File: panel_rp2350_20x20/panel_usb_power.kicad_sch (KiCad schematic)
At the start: 4 parts, among them J1 Conn_01x04, U39 AP2112K-3.3

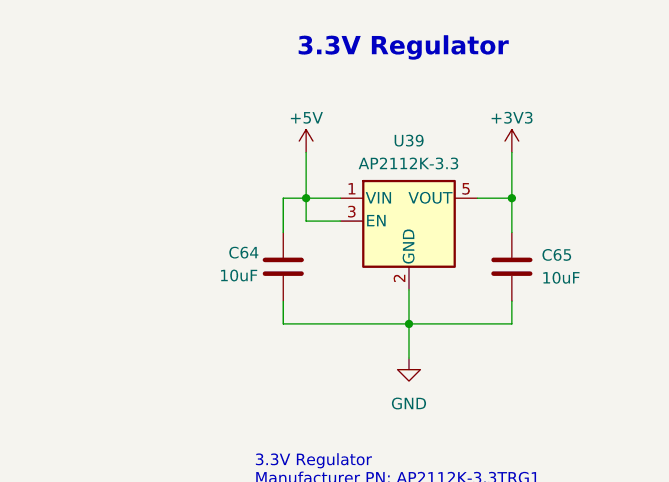
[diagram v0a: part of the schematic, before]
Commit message: More work on rp2350 20x20 panel.
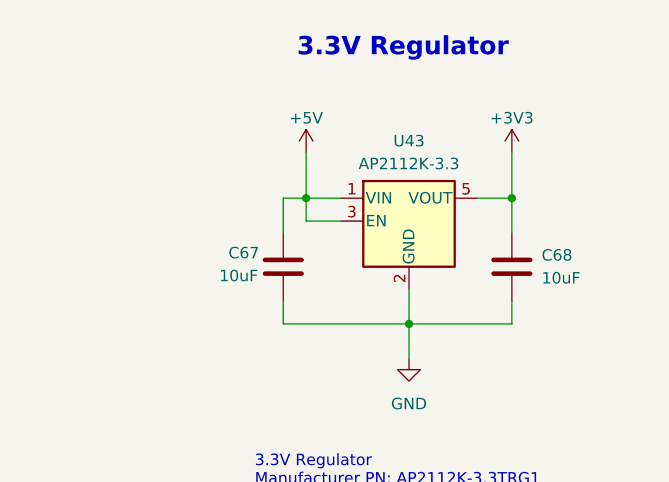
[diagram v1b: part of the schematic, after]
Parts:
- renumbered C64 to C67, C65 to C68, U39 to U43
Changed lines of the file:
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@@
 		(dnp no)
 		(fields_autoplaced yes)
-		(property "Reference" "#PWR0110"
+		(property "Reference" "#PWR0118"
 			(at 100.965 59.69 0)
 			(effects
@@
 			(project "driver_rp2350"
 				(path "/1e634561-32a0-4ffa-9d4f-e93f355464d5/e614504e-e15b-412a-a899-de4ba0827a39"
-					(reference "#PWR0110")
+					(reference "#PWR0118")
 					(unit 1)
 				)
@@
 		(dnp no)
 		(fields_autoplaced yes)
-		(property "Reference" "#PWR0113"
+		(property "Reference" "#PWR0121"
 			(at 226.06 44.45 0)
 			(effects
@@
 			(project "driver_rp2350"
 				(path "/1e634561-32a0-4ffa-9d4f-e93f355464d5/e614504e-e15b-412a-a899-de4ba0827a39"
-					(reference "#PWR0113")
+					(reference "#PWR0121")
 					(unit 1)
 				)
@@
 		(on_board yes)
 		(dnp no)
-		(property "Reference" "#PWR0109"
+		(property "Reference" "#PWR0117"
 			(at 100.965 48.895 0)
 			(effects
@@
 			(project "driver_rp2350"
 				(path "/1e634561-32a0-4ffa-9d4f-e93f355464d5/e614504e-e15b-412a-a899-de4ba0827a39"
-					(reference "#PWR0109")
+					(reference "#PWR0117")
 					(unit 1)
 				)
@@
 		(on_board yes)
 		(dnp no)
-		(property "Reference" "#PWR0111"
+		(property "Reference" "#PWR0119"
 			(at 203.2 44.45 0)
 			(effects
@@
 			(project "driver_rp2350"
 				(path "/1e634561-32a0-4ffa-9d4f-e93f355464d5/e614504e-e15b-412a-a899-de4ba0827a39"
-					(reference "#PWR0111")
+					(reference "#PWR0119")
 					(unit 1)
 				)
@@
 		(on_board yes)
 		(dnp no)
-		(property "Reference" "C64"
+		(property "Reference" "C67"
 			(at 194.564 51.816 0)
 			(effects
@@
 			(project "driver_rp2350"
 				(path "/1e634561-32a0-4ffa-9d4f-e93f355464d5/e614504e-e15b-412a-a899-de4ba0827a39"
-					(reference "C64")
+					(reference "C67")
 					(unit 1)
 				)
@@
 		(on_board yes)
 		(dnp no)
-		(property "Reference" "C65"
+		(property "Reference" "C68"
 			(at 229.362 52.07 0)
 			(effects
@@
 			(project "driver_rp2350"
 				(path "/1e634561-32a0-4ffa-9d4f-e93f355464d5/e614504e-e15b-412a-a899-de4ba0827a39"
-					(reference "C65")
+					(reference "C68")
 					(unit 1)
 				)
@@
 		(dnp no)
 		(fields_autoplaced yes)
-		(property "Reference" "U39"
+		(property "Reference" "U43"
 			(at 214.63 39.37 0)
 			(effects
@@
 			(project "driver_rp2350"
 				(path "/1e634561-32a0-4ffa-9d4f-e93f355464d5/e614504e-e15b-412a-a899-de4ba0827a39"
-					(reference "U39")
+					(reference "U43")
 					(unit 1)
 				)
@@
 		(dnp no)
 		(fields_autoplaced yes)
-		(property "Reference" "#PWR0112"
+		(property "Reference" "#PWR0120"
 			(at 214.63 69.85 0)
 			(effects
@@
 			(project "driver_rp2350"
 				(path "/1e634561-32a0-4ffa-9d4f-e93f355464d5/e614504e-e15b-412a-a899-de4ba0827a39"
-					(reference "#PWR0112")
-					(unit 1)
-				)
+					(reference "#PWR0120")
+					(unit 1)
+				)

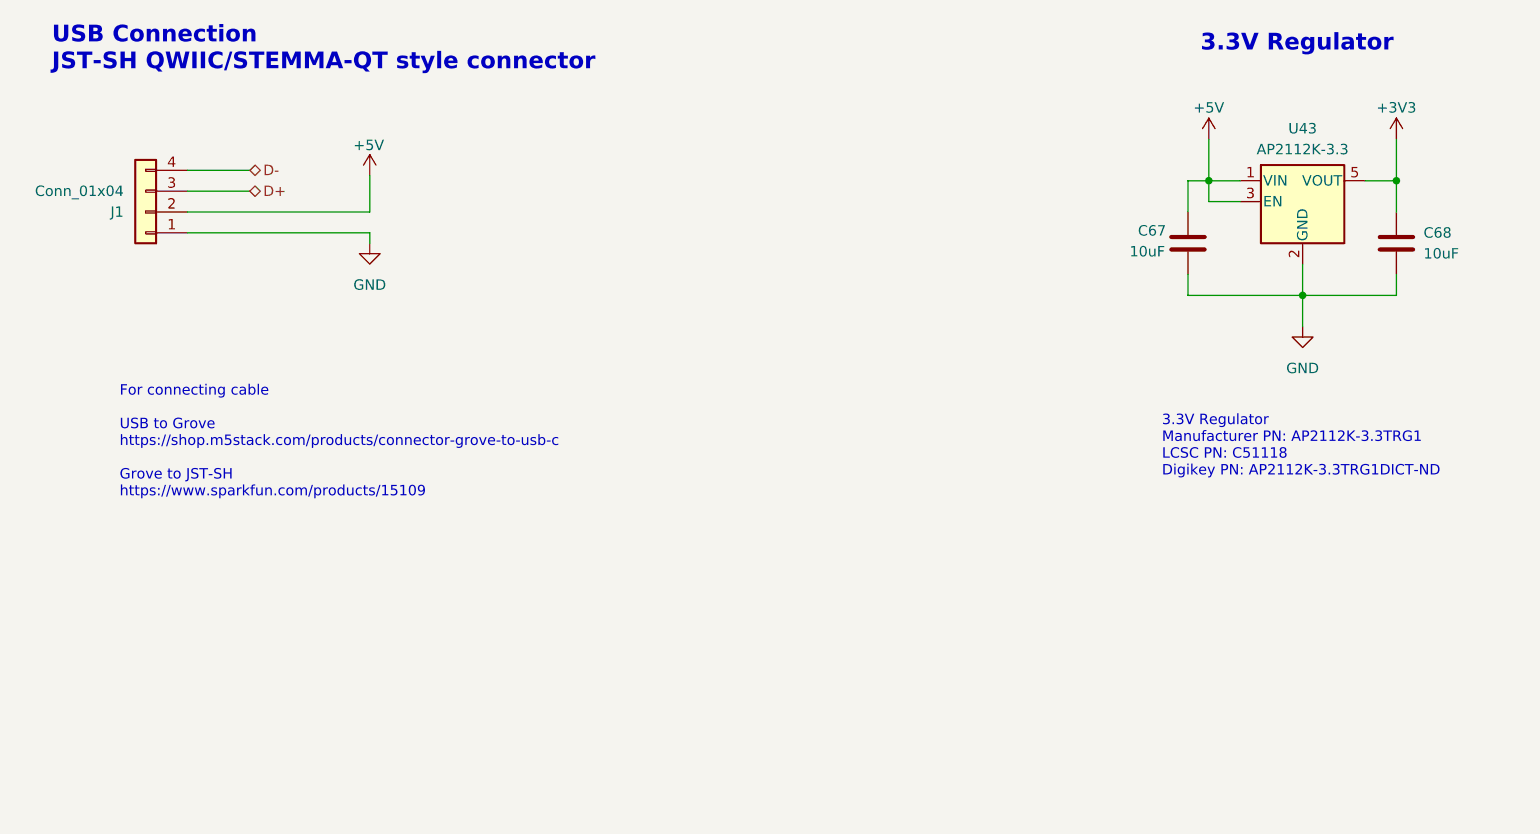
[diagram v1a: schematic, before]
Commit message: Worked on rp2350 20x20 panel layout and routing.
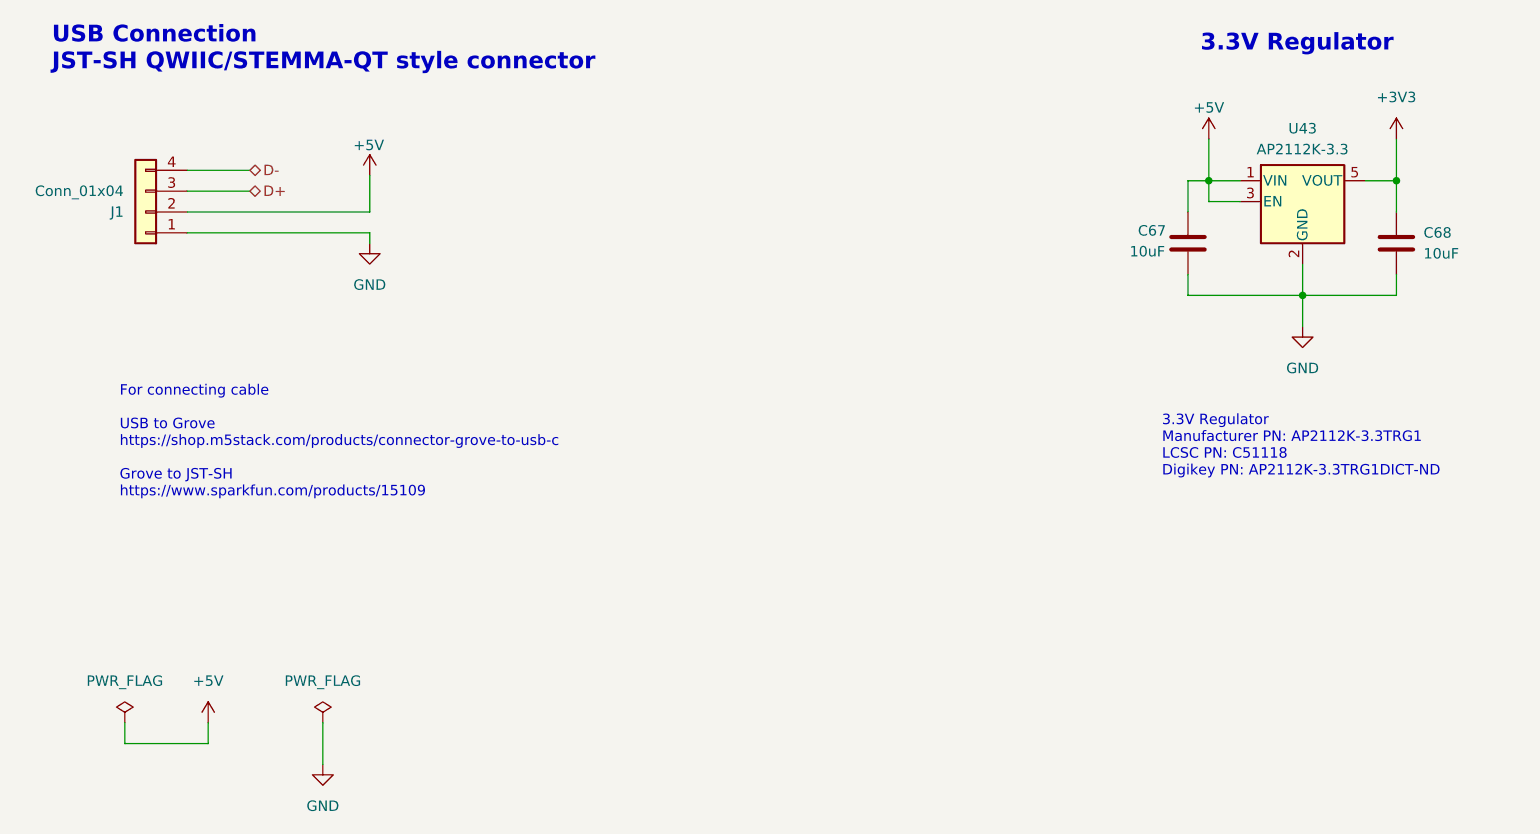
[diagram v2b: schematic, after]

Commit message: Worked on setup for fabrication.
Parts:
- U43: LCSC Part # (none) -> C51118
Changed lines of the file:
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@@
+			)
+		)
+		(property "LCSC Part #" "C51118"
+			(at 214.63 48.26 0)
+			(effects
+				(font
+					(size 1.27 1.27)
+				)
 			)
 		)

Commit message: Worked on fab files.
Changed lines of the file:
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@@
 					(size 1.27 1.27)
 				)
+				(hide yes)
 			)
 		)

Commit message: Worked on routing and fabrication setup.
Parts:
- C67, C68: LCSC Part # (none) -> C315248
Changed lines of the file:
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@@
 					(size 1.27 1.27)
 				)
+				(hide yes)
+			)
+		)
+		(property "LCSC Part #" "C315248"
+			(at 200.66 53.34 0)
+			(effects
+				(font
+					(size 1.27 1.27)
+				)
+				(hide yes)
 			)
 		)
@@
 					(size 1.27 1.27)
 				)
+				(hide yes)
+			)
+		)
+		(property "LCSC Part #" "C315248"
+			(at 226.06 53.34 0)
+			(effects
+				(font
+					(size 1.27 1.27)
+				)
+				(hide yes)
 			)
 		)
@@
 					(size 1.27 1.27)
 				)
-			)
-		)
+				(hide yes)
+			)
+		)

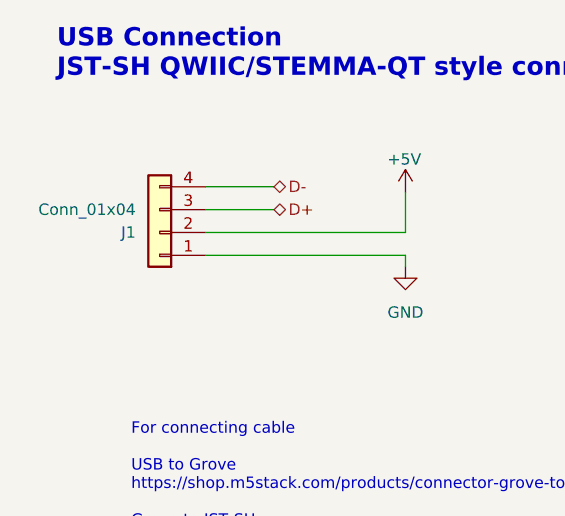
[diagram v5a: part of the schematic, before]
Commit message: Worked on routing, layout and fab setup for rp2354b 20x20 panel.
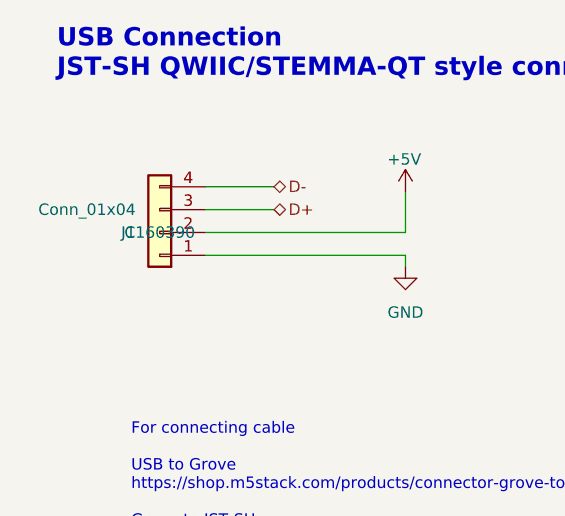
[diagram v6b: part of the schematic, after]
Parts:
- J1: LCSC Part # (none) -> C160390
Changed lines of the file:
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@@
+			)
+		)
+		(property "LCSC Part #" "C160390"
+			(at 73.66 49.53 0)
+			(effects
+				(font
+					(size 1.27 1.27)
+				)
 			)
 		)
